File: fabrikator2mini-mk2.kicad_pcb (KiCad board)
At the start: 2 copper layers, 122 parts, among them CON1 Micro_SD_Card, J1 USB_OTG, J10 END_X/ESP, J11 MT_Y, J12 Conn_01x12, J13 Z, J14 MT_Z, J15 B, J16 BTN1, J17 Fan1, J2 RESET, J3 PWR_IN, J4 B, J5 I2C, J6 SWD, J7 SPI, J8 Fan2, J9 MT_X, P16 SW_DIP, P17 SW_DIP, P18 SW_DIP, P19 SW_DIP, Q1 PSMN2R4-30MLD, Q2 PSMN2R4-30MLD, Q3 PSMN2R4-30MLD, Q4 PSMN2R4-30MLD, Q5 Si7145DP, U1 bluepill, U2 CPDT6-5V4, U3 CPDT6-5V4, U4 4988, U5 4988, U6 4988, U7 4988, U8 L7812, U9 TS30011

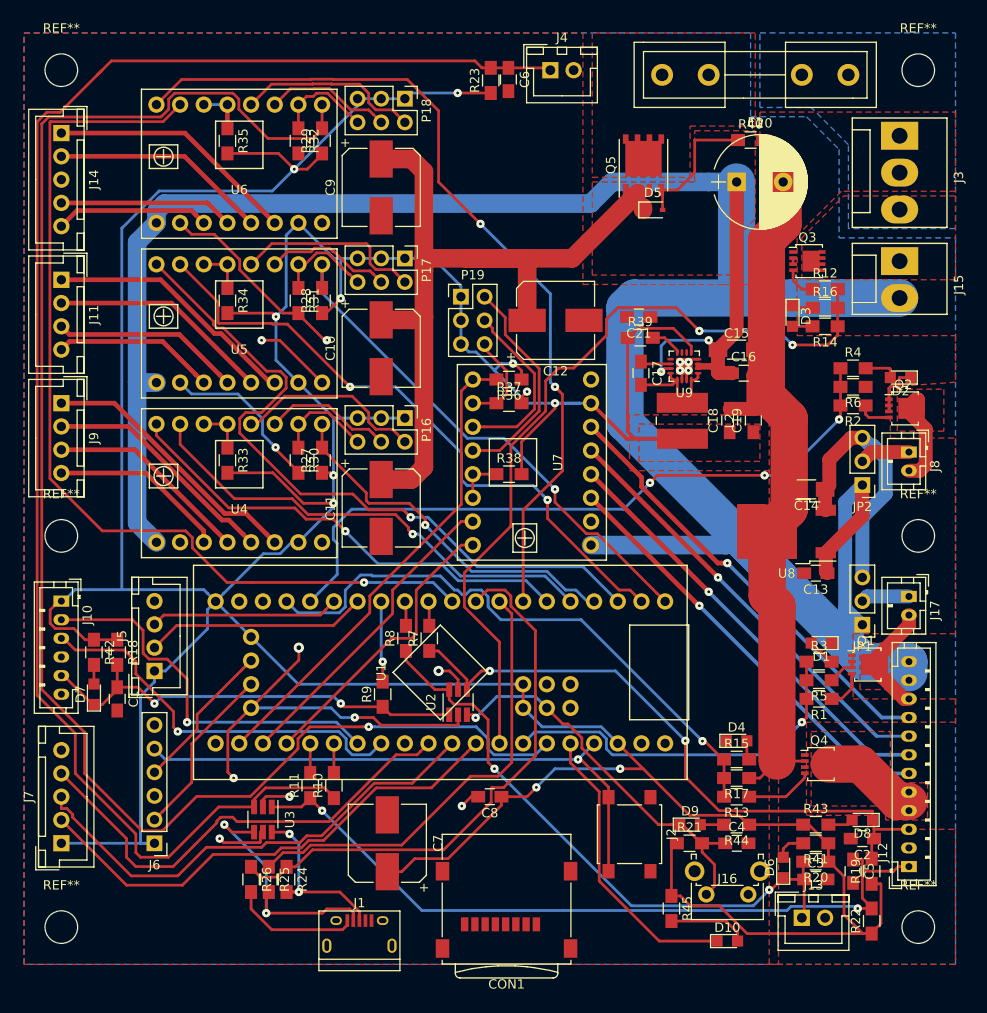
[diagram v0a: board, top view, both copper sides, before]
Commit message: rerouted and removed 12V
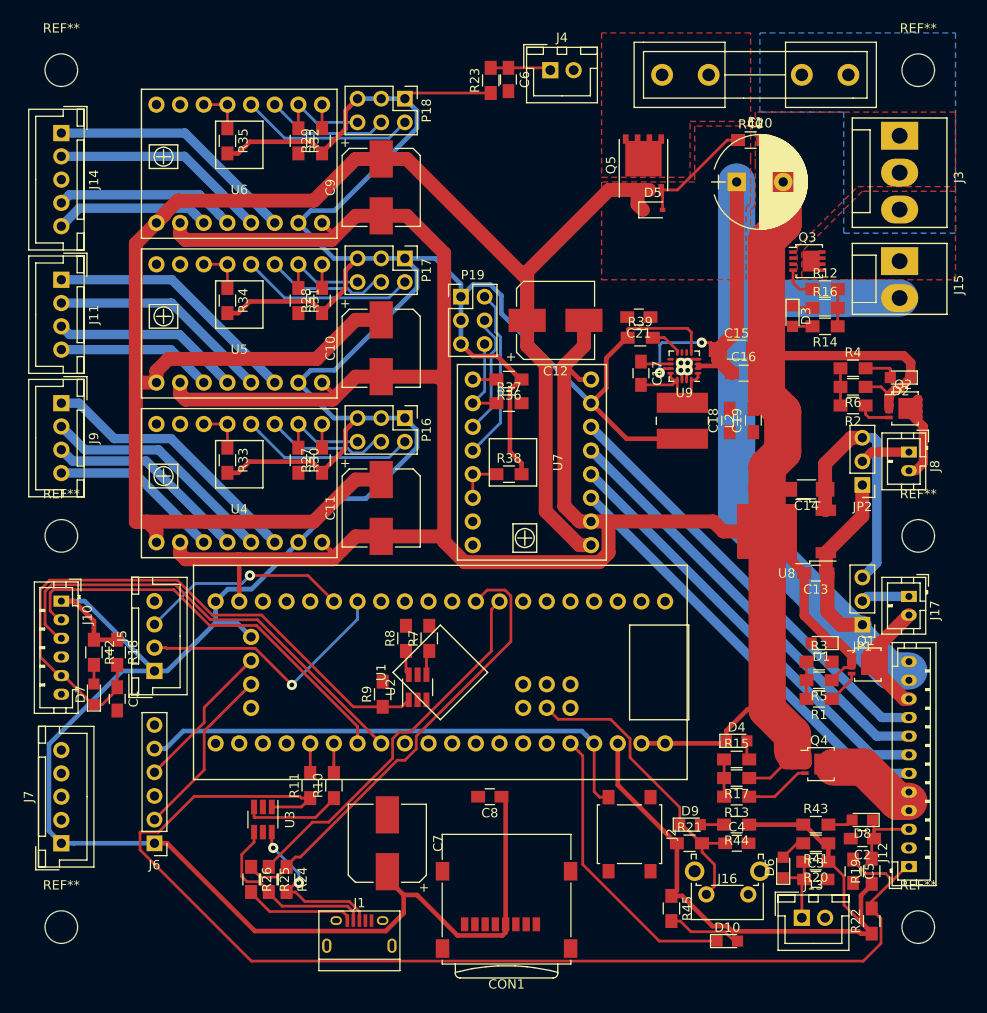
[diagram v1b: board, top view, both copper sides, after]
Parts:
- moved U2 4.63 mm to (62.2, 90.2)
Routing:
- net Z_EN: track 169.3 -> 2.54 mm, vias 1 -> 0
- net GND: track 203.2 -> 355.3 mm, vias 15 -> 4
- net BED_SENSE: track 167.7 -> 17.1 mm
- net Z_STEP: track 102.3 -> 0.00 mm, vias 1 -> 0
- net Z_DIR: track 92.8 -> 0.00 mm, vias 2 -> 0
- net HEAT_BED: track 87.0 -> 4.00 mm, vias 2 -> 0
- net Y_DIR: track 76.3 -> 0.00 mm, vias 1 -> 0
- net FAN2: track 74.0 -> 4.00 mm, vias 3 -> 0
- net Y_STEP: track 68.7 -> 0.00 mm, vias 2 -> 0
- net HOTEND: track 63.5 -> 4.00 mm, vias 1 -> 0
- net VCC: track 394.2 -> 335.8 mm
- net END_Y: track 68.5 -> 11.7 mm, vias 2 -> 0
- net Y_EN: track 57.0 -> 2.54 mm, vias 1 -> 0
- net END_Z: track 65.5 -> 11.2 mm, vias 2 -> 0
- net SD_CMD: track 53.7 -> 0.00 mm
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- removed copper zone on F.Cu, net +3V3
- removed copper zone on F.Cu, net FAN1_PWR
- removed copper zone on F.Cu, net FAN2_PWR
- removed copper zone on B.Cu, net GND
- removed copper zone on F.Cu, net HOTEND_PWR

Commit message: rc1 route
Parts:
- removed C13: 0.33u/35V, Capacitors_SMD:C_0805_HandSoldering
- removed C14: 10u/35V, Capacitors_SMD:C_1206_HandSoldering
- removed JP1: FAN1 PWR SEL, Pin_Headers:Pin_Header_Straight_1x03_Pitch2.54mm
- removed JP2: FAN2 PWR SEL, Pin_Headers:Pin_Header_Straight_1x03_Pitch2.54mm
- removed U8: L7812, TO_SOT_Packages_SMD:TO-252-2
- moved R33 1.91 mm to (43.1, 64.5), turned to 0 degrees
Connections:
- J17 pad 1: Net-(J17-Pad1) -> VCC
- J8 pad 1: Net-(J8-Pad1) -> VCC
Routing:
- net GND: track 355.3 -> 882.9 mm, vias 4 -> 11
- net BED_SENSE: track 17.1 -> 170.1 mm
- net Z_DIR: track 0.00 -> 110.9 mm, vias 0 -> 3
- net Z_EN: track 2.54 -> 113.1 mm, vias 0 -> 1
- net Z_STEP: track 0.00 -> 86.6 mm
- net FAN2: track 4.00 -> 81.2 mm, vias 0 -> 4
- net SD_CLK: track 0.00 -> 76.1 mm, vias 0 -> 1
- net SD_CMD: track 0.00 -> 75.5 mm, vias 0 -> 1
- net HEAT_BED: track 4.00 -> 77.2 mm, vias 0 -> 3
- net SD_DAT0: track 0.00 -> 72.1 mm, vias 0 -> 1
- net Y_DIR: track 0.00 -> 69.2 mm, vias 0 -> 2
- net Y_STEP: track 0.00 -> 68.2 mm, vias 0 -> 2
- net END_Z: track 11.2 -> 75.9 mm, vias 0 -> 2
- net Y_EN: track 2.54 -> 62.8 mm, vias 0 -> 1
- net END_Y: track 11.7 -> 69.5 mm, vias 0 -> 2
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- added copper zone on B.Cu, net GND
- added copper zone on B.Cu, net VCC
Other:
- board outline added: 100 x 100 mm

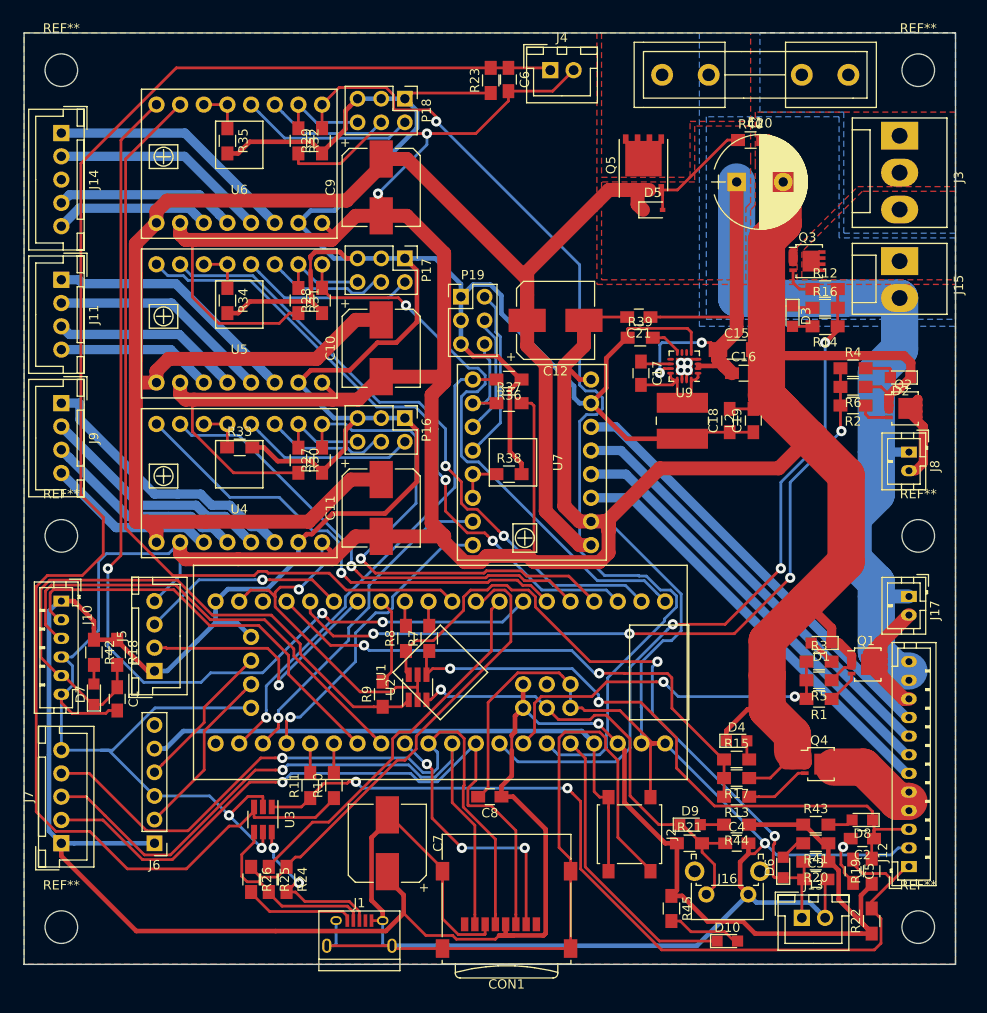
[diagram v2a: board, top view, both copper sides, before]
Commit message: Power routing and stepper driver signals routed after MCU rotation
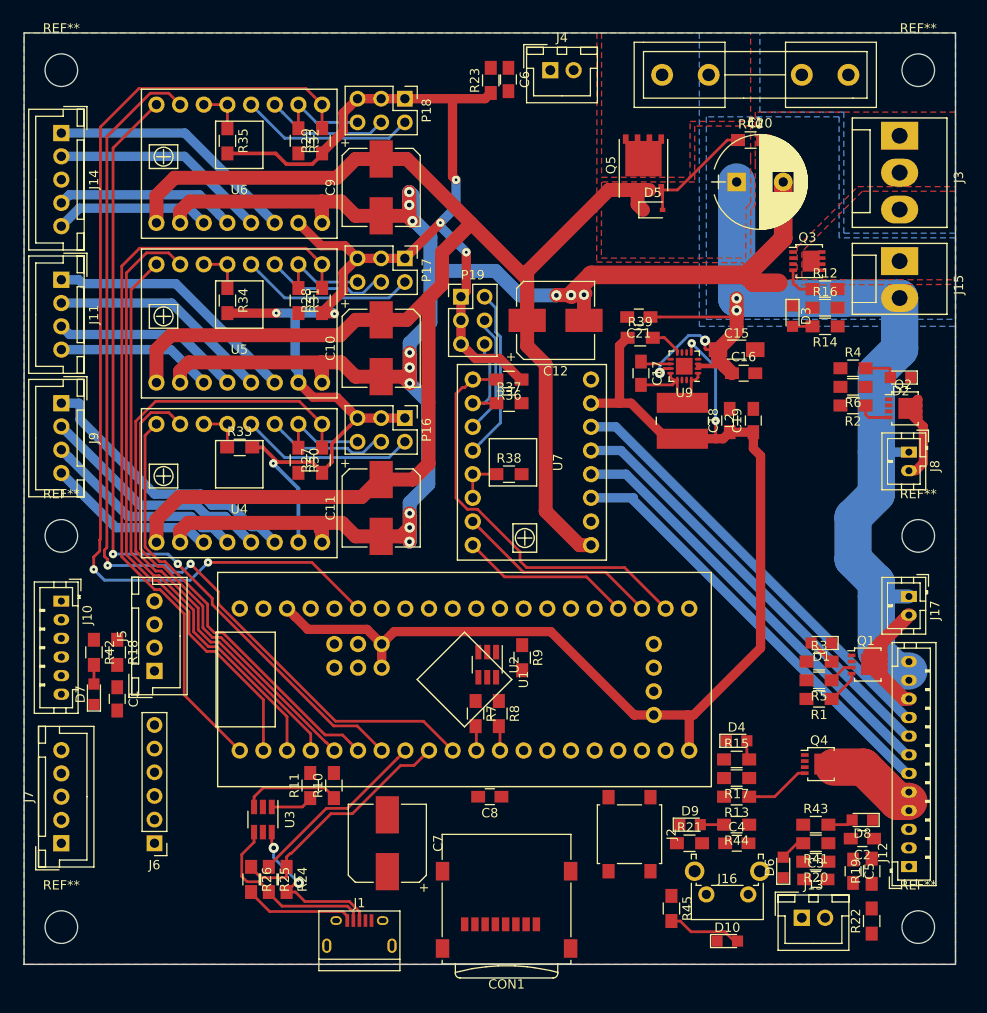
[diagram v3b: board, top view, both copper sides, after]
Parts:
- moved R9 15.5 mm to (73.5, 87.1), turned to 270 degrees
- moved R8 12.8 mm to (71.0, 93.1), turned to 270 degrees
- moved R7 9.48 mm to (68.5, 93.1), turned to 270 degrees
- moved U2 7.86 mm to (69.7, 87.8), turned to 270 degrees
- moved U1 2.70 mm to (67.3, 89.4), turned to 90 degrees
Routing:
- net GND: track 882.9 -> 201.4 mm, vias 11 -> 12
- net +3V3: track 514.3 -> 284.0 mm, vias 1 -> 8
- net BED_SENSE: track 170.1 -> 10.6 mm
- net HOTEND_SENSE: track 94.5 -> 4.58 mm, vias 2 -> 0
- net FAN2: track 81.2 -> 0.00 mm, vias 4 -> 0
- net HEAT_BED: track 77.2 -> 0.00 mm, vias 3 -> 0
- net SD_CLK: track 76.1 -> 0.00 mm, vias 1 -> 0
- net END_Z: track 75.9 -> 0.00 mm, vias 2 -> 0
- net SD_CMD: track 75.5 -> 0.00 mm, vias 1 -> 0
- net SD_DAT0: track 72.1 -> 0.00 mm, vias 1 -> 0
- net END_Y: track 69.5 -> 0.00 mm, vias 2 -> 0
- net END_X: track 67.4 -> 0.00 mm
- net RESET: track 63.5 -> 0.00 mm
- net HOTEND: track 59.9 -> 0.00 mm, vias 2 -> 0
- net BTN1: track 49.7 -> 0.00 mm, vias 1 -> 0
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
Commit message: Route most nets
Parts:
- moved J6 70.7 mm to (97.3, 75.5), turned to 270 degrees
- moved C8 17.7 mm to (82.8, 114.2), turned to 0 degrees
- moved R9 1.39 mm to (74.7, 87.8)
- moved C15 0.49 mm to (97.0, 53.9)
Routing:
- net GND: track 201.4 -> 444.1 mm, vias 12 -> 51
- net +3V3: track 284.0 -> 487.5 mm, vias 8 -> 17
- net BED_SENSE: track 10.6 -> 169.9 mm
- net RESET: track 0.00 -> 122.3 mm, vias 0 -> 6
- net SD_CLK: track 0.00 -> 105.3 mm, vias 0 -> 6
- net SD_CMD: track 0.00 -> 95.7 mm, vias 0 -> 4
- net LED1: track 0.00 -> 92.1 mm, vias 0 -> 4
- net HOTEND_SENSE: track 4.58 -> 92.9 mm, vias 0 -> 2
- net SD_DAT0: track 0.00 -> 82.2 mm, vias 0 -> 4
- net HEAT_BED: track 0.00 -> 77.9 mm, vias 0 -> 4
- net END_X: track 0.00 -> 69.5 mm, vias 0 -> 4
- net BTN1: track 0.00 -> 66.2 mm, vias 0 -> 2
- net END_Y: track 0.00 -> 63.5 mm
- net FAN2: track 0.00 -> 62.9 mm, vias 0 -> 1
- net ESP_TX: track 0.00 -> 57.4 mm, vias 0 -> 3
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
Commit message: Fully routed
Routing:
- net GND: track 444.1 -> 474.2 mm, vias 51 -> 53
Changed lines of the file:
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@@
   (general
     (links 342)
-    (no_connects 6)
+    (no_connects 1)
     (area 15.871429 18.445 124.128572 123.215)
     (thickness 1.6)
     (drawings 11)
-    (tracks 1644)
+    (tracks 1671)
     (zones 0)
     (modules 117)
@@
   (segment (start 27.35 92.1) (end 27.5 92.1) (width 0.3) (layer F.Cu) (net 1))
   (segment (start 70.675 86.475) (end 74.65 86.475) (width 0.3) (layer F.Cu) (net 1))
+  (segment (start 57.3 115.3) (end 57.3 115.775) (width 0.3) (layer F.Cu) (net 2))
+  (segment (start 57.3 115.775) (end 59.5 117.975) (width 0.3) (layer F.Cu) (net 2))
+  (segment (start 59.5 117.975) (end 59.5 118) (width 0.3) (layer F.Cu) (net 2))
+  (segment (start 57.3 115.3) (end 58.5 115.3) (width 0.3) (layer F.Cu) (net 2))
+  (segment (start 108.75 106.5) (end 108.625 106.5) (width 0.3) (layer F.Cu) (net 2))
+  (segment (start 108.625 106.5) (end 107.975 107.15) (width 0.3) (layer F.Cu) (net 2))
+  (segment (start 107.975 107.15) (end 107.975 110.125) (width 0.3) (layer F.Cu) (net 2))
+  (segment (start 107.975 110.125) (end 109 111.15) (width 0.3) (layer F.Cu) (net 2))
+  (segment (start 109 111.15) (end 109 111.25) (width 0.3) (layer F.Cu) (net 2))
+  (segment (start 96.87 108.825) (end 96.87 111.61) (width 0.3) (layer F.Cu) (net 2))
+  (segment (start 96.87 111.61) (end 97.75 112.49) (width 0.3) (layer F.Cu) (net 2))
+  (segment (start 97.77 107) (end 97.77 107.925) (width 0.3) (layer F.Cu) (net 2))
+  (segment (start 97.77 107.925) (end 96.87 108.825) (width 0.3) (layer F.Cu) (net 2))
+  (segment (start 95.4 96) (end 96.749999 97.349999) (width 0.3) (layer F.Cu) (net 2))
+  (segment (start 96.749999 97.349999) (end 96.749999 98.999999) (width 0.3) (layer F.Cu) (net 2))
+  (segment (start 96.749999 98.999999) (end 97.75 100) (width 0.3) (layer F.Cu) (net 2))
+  (segment (start 97.75 100) (end 97.85 100) (width 0.3) (layer F.Cu) (net 2))
+  (segment (start 45.6413 103.1012) (end 45.6413 102.0212) (width 0.3) (layer F.Cu) (net 2))
+  (segment (start 45.591299 101.971199) (end 43.203801 101.971199) (width 0.3) (layer F.Cu) (net 2))
+  (segment (start 45.6413 102.0212) (end 45.591299 101.971199) (width 0.3) (layer F.Cu) (net 2))
+  (segment (start 43.203801 101.971199) (end 43.1 102.075) (width 0.3) (layer F.Cu) (net 2))
+  (via (at 43.1 102.075) (size 0.9) (drill 0.3) (layers F.Cu B.Cu) (net 2))
+  (segment (start 44.975 107.825) (end 42.6 107.825) (width 0.3) (layer B.Cu) (net 2))
+  (segment (start 45.6413 105.8012) (end 45.6413 107.1587) (width 0.3) (layer F.Cu) (net 2))
+  (segment (start 45.6413 107.1587) (end 44.975 107.825) (width 0.3) (layer F.Cu) (net 2))
+  (via (at 44.975 107.825) (size 0.9) (drill 0.3) (layers F.Cu B.Cu) (net 2))
   (segment (start 77.775 77.338604) (end 77.775 75.5475) (width 0.3) (layer B.Cu) (net 2))
   (segment (start 77.775 75.5475) (end 80.8713 72.4512) (width 0.3) (layer B.Cu) (net 2))
@@
   (via (at 96.5 48.5) (size 1.1) (drill 0.5) (layers F.Cu B.Cu) (net 8))
   (segment (start 63.4225 66.2525) (end 61.7238 67.9512) (width 1.5) (layer F.Cu) (net 8))
+  (segment (start 63.4225 48.475) (end 63.4225 66.2525) (width 1.5) (layer F.Cu) (net 8))
   (segment (start 61.7238 67.9512) (end 58.3413 67.9512) (width 1.5) (layer F.Cu) (net 8))
   (segment (start 63.4225 48.475) (end 64.875 47.0225) (width 1.5) (layer F.Cu) (net 8))
   (segment (start 61.0913 50.8062) (end 63.4225 48.475) (width 1.5) (layer F.Cu) (net 8))
-  (segment (start 63.4225 48.475) (end 63.4225 66.2525) (width 1.5) (layer F.Cu) (net 8))
   (segment (start 61.0913 33.5362) (end 68.0051 40.45) (width 1.5) (layer F.Cu) (net 8))
   (segment (start 68.0051 40.45) (end 74.0113 46.4562) (width 1.5) (layer F.Cu) (net 8))
@@
   (segment (start 92.355 56.985) (end 92.08 57.26) (width 0.3) (layer F.Cu) (net 10))
   (segment (start 92.355 56.535) (end 92.355 56.985) (width 0.3) (layer F.Cu) (net 10) (status 10))
+  (segment (start 109.75 112.85) (end 107.831385 110.931385) (width 0.3) (layer B.Cu) (net 11))
+  (segment (start 107.4 109.9262) (end 107.4 110.681385) (width 0.3) (layer F.Cu) (net 11))
+  (segment (start 106.35 108.9762) (end 106.45 108.9762) (width 0.3) (layer F.Cu) (net 11))
+  (segment (start 106.45 108.9762) (end 107.4 109.9262) (width 0.3) (layer F.Cu) (net 11))
+  (segment (start 107.831385 110.931385) (end 107.65 110.931385) (width 0.3) (layer B.Cu) (net 11))
+  (segment (start 107.4 110.681385) (end 107.65 110.931385) (width 0.3) (layer F.Cu) (net 11))
+  (via (at 107.65 110.931385) (size 0.9) (drill 0.3) (layers F.Cu B.Cu) (net 11))
   (segment (start 86.728701 92.353801) (end 87.6037 93.2288) (width 1) (layer F.Cu) (net 11))
   (segment (start 80.247998 89.025002) (end 83.399902 89.025002) (width 1) (layer F.Cu) (net 11))
@@
   (segment (start 109.75 116.4) (end 109.75 113.486396) (width 0.3) (layer F.Cu) (net 11))
   (segment (start 109.75 113.486396) (end 109.75 112.85) (width 0.3) (layer F.Cu) (net 11))
-  (segment (start 107.629036 110.092441) (end 107.466241 110.092441) (width 0.3) (layer F.Cu) (net 11))
-  (segment (start 107.466241 110.092441) (end 106.35 108.9762) (width 0.3) (layer F.Cu) (net 11))
-  (segment (start 107.6 110.7) (end 107.6 110.121477) (width 0.3) (layer B.Cu) (net 11))
-  (segment (start 107.6 110.121477) (end 107.629036 110.092441) (width 0.3) (layer B.Cu) (net 11))
-  (via (at 107.629036 110.092441) (size 0.9) (drill 0.3) (layers F.Cu B.Cu) (net 11))
-  (segment (start 109.75 112.85) (end 107.6 110.7) (width 0.3) (layer B.Cu) (net 11))
   (segment (start 111 111.35) (end 111 111.6) (width 0.3) (layer F.Cu) (net 11))
   (segment (start 111 111.6) (end 109.75 112.85) (width 0.3) (layer F.Cu) (net 11))

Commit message: silkscreen work
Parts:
- added G***: LOGO, fabrikator2mini-mk2:radiona, F.Cu at (90.2, 45.8)
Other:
- board text added: "3.3V"
- board text added: "BED P"
- board text added: "BED S"
- board text added: "DEBUG"
- board text added: "FAN1"
- board text added: "FAN2"
- board text added: "Fabrikator ][ mini replacement board"
- board text added: "GND"
- board text added: "I²C"
- board text added: "NRST"
- board text added: "POWER"
- board text added: "SB"
- board text added: "SPI"
- board text added: "SWCLK"
- board text added: "SWDIO"
- board text added: "SWO"
- board text added: "V1"
- board text added: "Vcc"
- board text added: "X"
- board text added: "Y"
- board text added: "Z"
- board text added: "sinister.io"
